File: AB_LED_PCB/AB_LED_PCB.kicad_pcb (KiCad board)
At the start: 2 copper layers, 49.1 x 21.4 mm, 15 parts, among them J1 Conn_01x03_Male

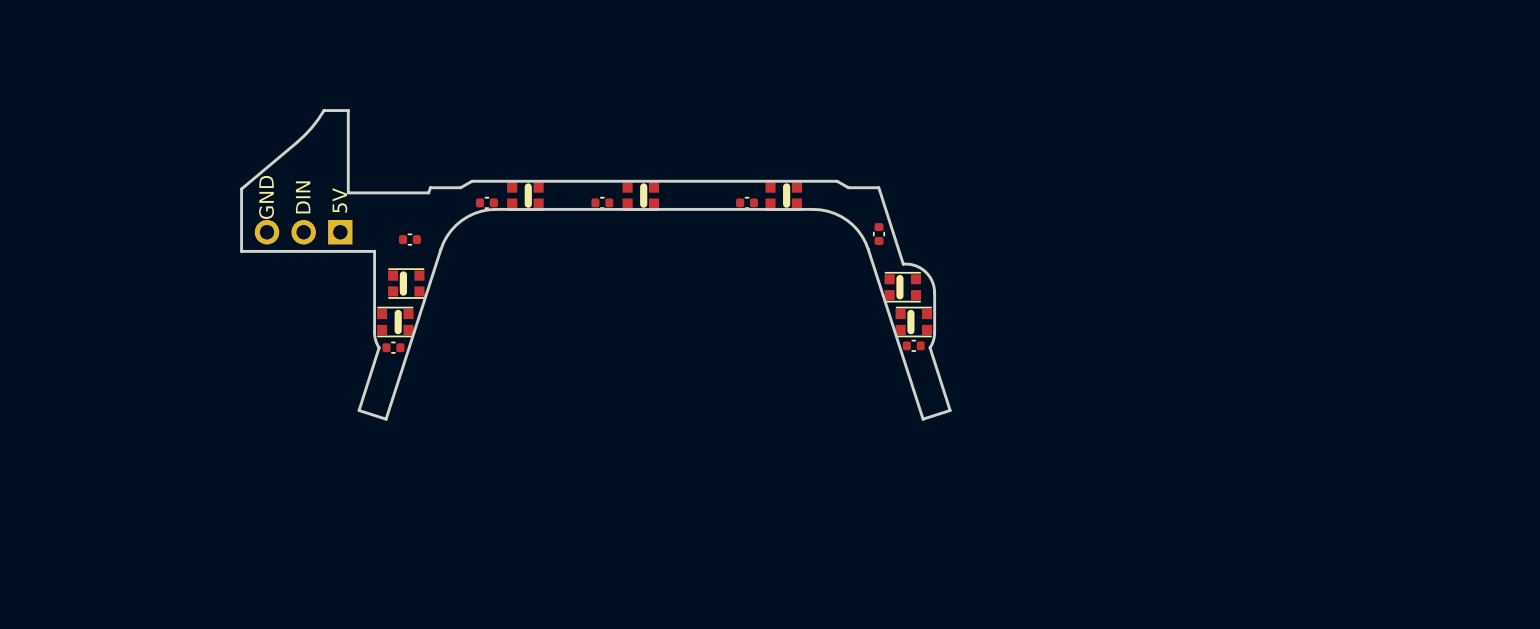
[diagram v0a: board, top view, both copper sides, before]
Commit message: added logo and routing
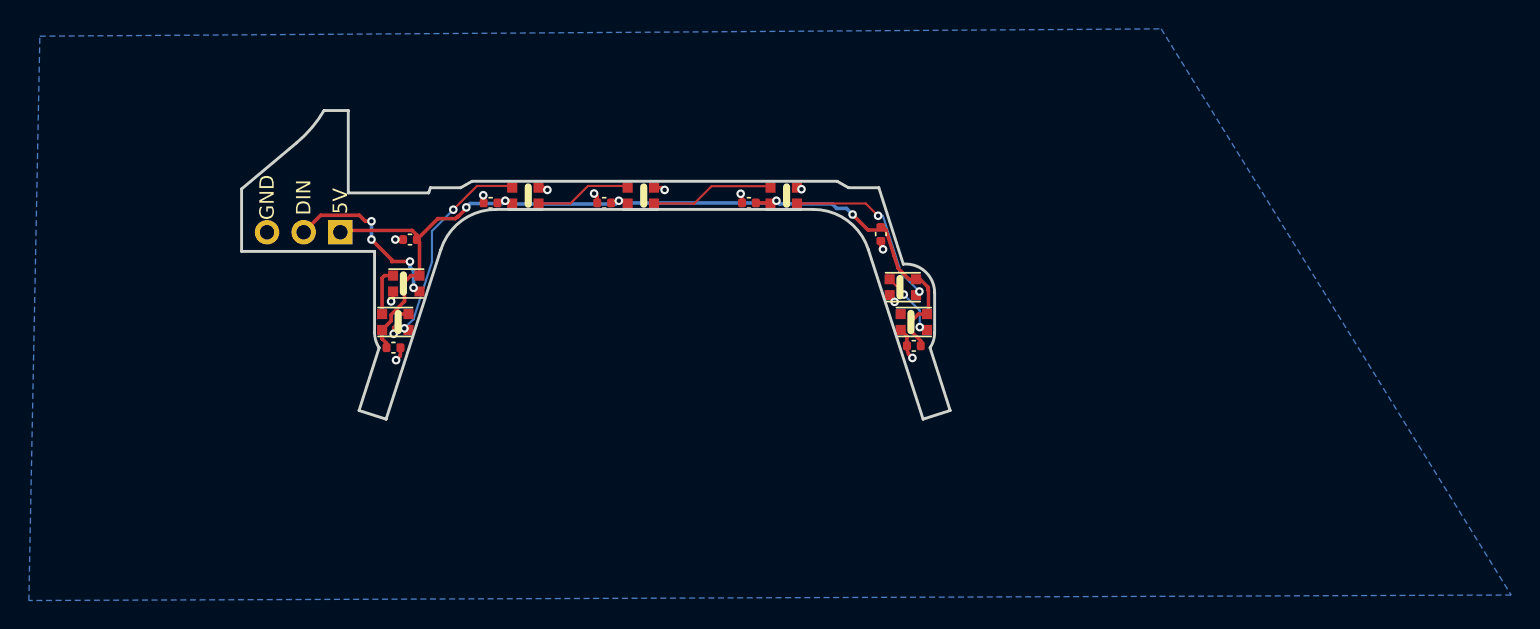
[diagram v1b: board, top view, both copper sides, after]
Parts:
- added SYM1: Logo_Open_Hardware_Small, Symbol:OSHW-Logo2_7.3x6mm_SilkScreen, B.Cu at (161.5, 103.2)
- moved C7 0.25 mm to (167.3, 101.0)
- moved C1 0.13 mm to (185.2, 101.0)
- moved C2 0.13 mm to (175.1, 101.0)
- moved C4 0.13 mm to (194.3, 103.1), turned to 270 degrees
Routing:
- net +5V: track 0.00 -> 64.4 mm, vias 0 -> 5
- net Net-(D6-Pad1): track 0.00 -> 14.4 mm, vias 0 -> 2
- net Net-(D2-Pad1): track 0.00 -> 12.7 mm, vias 0 -> 2
- net Net-(D5-Pad3): track 0.00 -> 12.4 mm, vias 0 -> 4
- net GND: track 0.00 -> 11.7 mm, vias 0 -> 13
- net Net-(D1-Pad1): track 0.00 -> 8.62 mm
- net Net-(D1-Pad3): track 0.00 -> 6.72 mm
- net Net-(D3-Pad1): track 0.00 -> 4.77 mm, vias 0 -> 2
- net Net-(D5-Pad1): track 0.00 -> 3.33 mm
- added copper zone on B.Cu, net GND
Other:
- net class Default: clearance 0.2 -> 0.15; via_dia 0.8 -> 0.6; via_drill 0.4 -> 0.3
- rule trace_clearance: 0.2 -> 0.15
- rule trace_min: 0.2 -> 0.15
- rule via_min_size: 0.4 -> 0.6

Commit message: fixed ercs
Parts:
- moved C4 0.06 mm to (194.2, 103.1)
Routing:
- added copper zone on F.Cu, net GND
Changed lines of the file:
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@@
     (thickness 1.6)
     (drawings 34)
-    (tracks 179)
+    (tracks 181)
     (zones 0)
     (modules 16)
@@
     (user_trace_width 0.15)
     (trace_clearance 0.15)
-    (zone_clearance 0.508)
+    (zone_clearance 0.25)
     (zone_45_only no)
     (trace_min 0.15)
@@
   )
   (module Capacitor_SMD:C_0402_1005Metric (layer F.Cu)
-    (at 194.31 103.124 270)
+    (at 194.2465 103.124 270)
     (descr "Capacitor SMD 0402 (1005 Metric), square (rectangular) end terminal, IPC_7351 nominal, (Body size source: IPC-SM-782 page 76, https://www.pcb-3d.com/wordpress/wp-content/uploads/ipc-sm-782a_amendment_1_and_2.pdf), generated with kicad-footprint-generator")
     (tags capacitor)
@@
   (segment (start 197.574432 106.850733) (end 197.557217 106.782293) (width 0.25) (layer F.Cu) (net 2))
   (segment (start 197.031924 106.257) (end 196.749 106.257) (width 0.25) (layer F.Cu) (net 2))
-  (segment (start 196.749 106.257) (end 196.265693 106.257) (width 0.25) (layer F.Cu) (net 2))
-  (segment (start 196.265693 106.257) (end 195.514072 105.505379) (width 0.25) (layer F.Cu) (net 2))
-  (segment (start 195.514072 105.505379) (end 195.242817 104.657999) (width 0.25) (layer F.Cu) (net 2))
-  (segment (start 194.660788 102.839788) (end 194.564 102.743) (width 0.25) (layer F.Cu) (net 2))
-  (segment (start 195.242817 104.657999) (end 194.660788 102.839788) (width 0.25) (layer F.Cu) (net 2))
   (segment (start 162.151 103.195) (end 162.151 103.505) (width 0.25) (layer F.Cu) (net 2))
   (segment (start 161.82599 102.86999) (end 162.151 103.195) (width 0.25) (layer F.Cu) (net 2))
@@
   (segment (start 187.071 100.81435) (end 186.916849 100.968501) (width 0.25) (layer B.Cu) (net 2))
   (segment (start 176.727415 100.968501) (end 176.573264 100.81435) (width 0.25) (layer B.Cu) (net 2))
-  (segment (start 194.660788 102.839788) (end 193.424024 102.839788) (width 0.25) (layer F.Cu) (net 2))
-  (segment (start 193.424024 102.839788) (end 192.352745 101.768509) (width 0.25) (layer F.Cu) (net 2))
-  (via (at 192.352745 101.768509) (size 0.6) (drill 0.3) (layers F.Cu B.Cu) (net 2))
-  (segment (start 191.252856 101.346) (end 191.930236 101.346) (width 0.25) (layer B.Cu) (net 2))
-  (segment (start 191.930236 101.346) (end 192.352745 101.768509) (width 0.25) (layer B.Cu) (net 2))
-  (segment (start 191.252856 101.346) (end 190.935356 101.0285) (width 0.25) (layer B.Cu) (net 2))
+  (via (at 192.316578 101.741269) (size 0.6) (drill 0.3) (layers F.Cu B.Cu) (net 2))
+  (segment (start 193.219309 102.644) (end 192.316578 101.741269) (width 0.25) (layer F.Cu) (net 2))
+  (segment (start 194.31 102.644) (end 193.219309 102.644) (width 0.25) (layer F.Cu) (net 2))
   (segment (start 187.28515 101.0285) (end 187.071 100.81435) (width 0.25) (layer B.Cu) (net 2))
-  (segment (start 190.935356 101.0285) (end 187.28515 101.0285) (width 0.25) (layer B.Cu) (net 2))
+  (segment (start 191.603809 101.0285) (end 187.28515 101.0285) (width 0.25) (layer B.Cu) (net 2))
+  (segment (start 192.316578 101.741269) (end 191.603809 101.0285) (width 0.25) (layer B.Cu) (net 2))
+  (segment (start 194.2465 102.644) (end 194.2465 102.6795) (width 0.25) (layer F.Cu) (net 2))
+  (segment (start 194.857595 103.290595) (end 194.8815 103.365275) (width 0.25) (layer F.Cu) (net 2))
+  (segment (start 194.2465 102.6795) (end 194.857595 103.290595) (width 0.25) (layer F.Cu) (net 2))
+  (segment (start 194.8815 103.365275) (end 194.8815 103.759) (width 0.25) (layer F.Cu) (net 2))
+  (segment (start 195.066878 103.944378) (end 195.453 105.150594) (width 0.25) (layer F.Cu) (net 2))
+  (segment (start 194.8815 103.759) (end 195.066878 103.944378) (width 0.25) (layer F.Cu) (net 2))
+  (segment (start 195.453 105.345202) (end 196.364798 106.257) (width 0.25) (layer F.Cu) (net 2))
+  (segment (start 196.364798 106.257) (end 196.749 106.257) (width 0.25) (layer F.Cu) (net 2))
+  (segment (start 195.453 105.150594) (end 195.453 105.345202) (width 0.25) (layer F.Cu) (net 2))
   (segment (start 170.587 101.007) (end 172.789992 101.007) (width 0.15) (layer F.Cu) (net 3))
   (segment (start 172.789992 101.007) (end 174.007633 99.789359) (width 0.15) (layer F.Cu) (net 3))
@@
     (polygon
       (pts
-        (xy 237.998 128.143) (xy 135.255 128.524) (xy 136.017 89.408) (xy 213.741 88.9)
+        (xy 200 120) (xy 145 120) (xy 145 95) (xy 200 95)
       )
     )
+  )
+  (zone (net 1) (net_name GND) (layer F.Cu) (hatch edge 0.508)
+    (connect_pads (clearance 0.25))
+    (min_thickness 0.2)
+    (fill yes (arc_segments 32) (thermal_gap 0.25) (thermal_bridge_width 0.25))
+    (polygon
+      (pts
+        (xy 200 120) (xy 145 120) (xy 145 95) (xy 200 95)
+      )
+    )
